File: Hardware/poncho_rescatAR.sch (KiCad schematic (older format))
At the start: 19 parts, among them P1 5V_OUT, P2 CONN_8, U1 LM317T, U2 LM7805

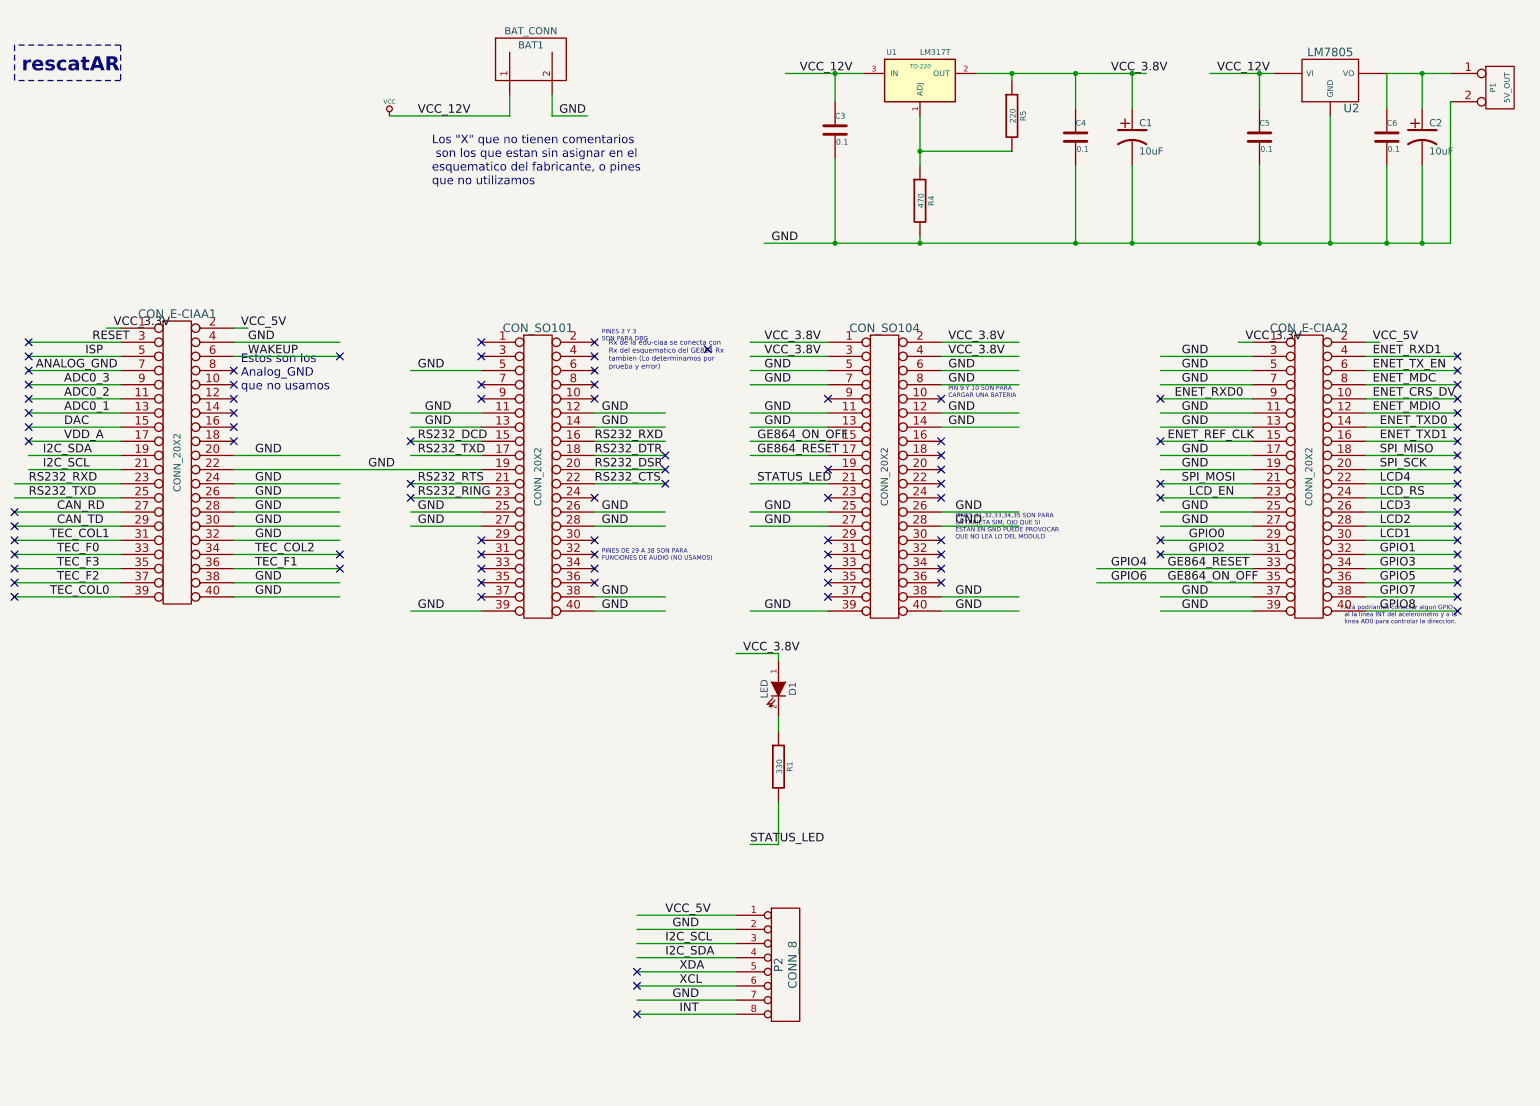
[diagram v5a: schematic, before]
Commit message: Agregado de capacitores en la alimentacion del acelerometro y pulsador de reset de la ciaa
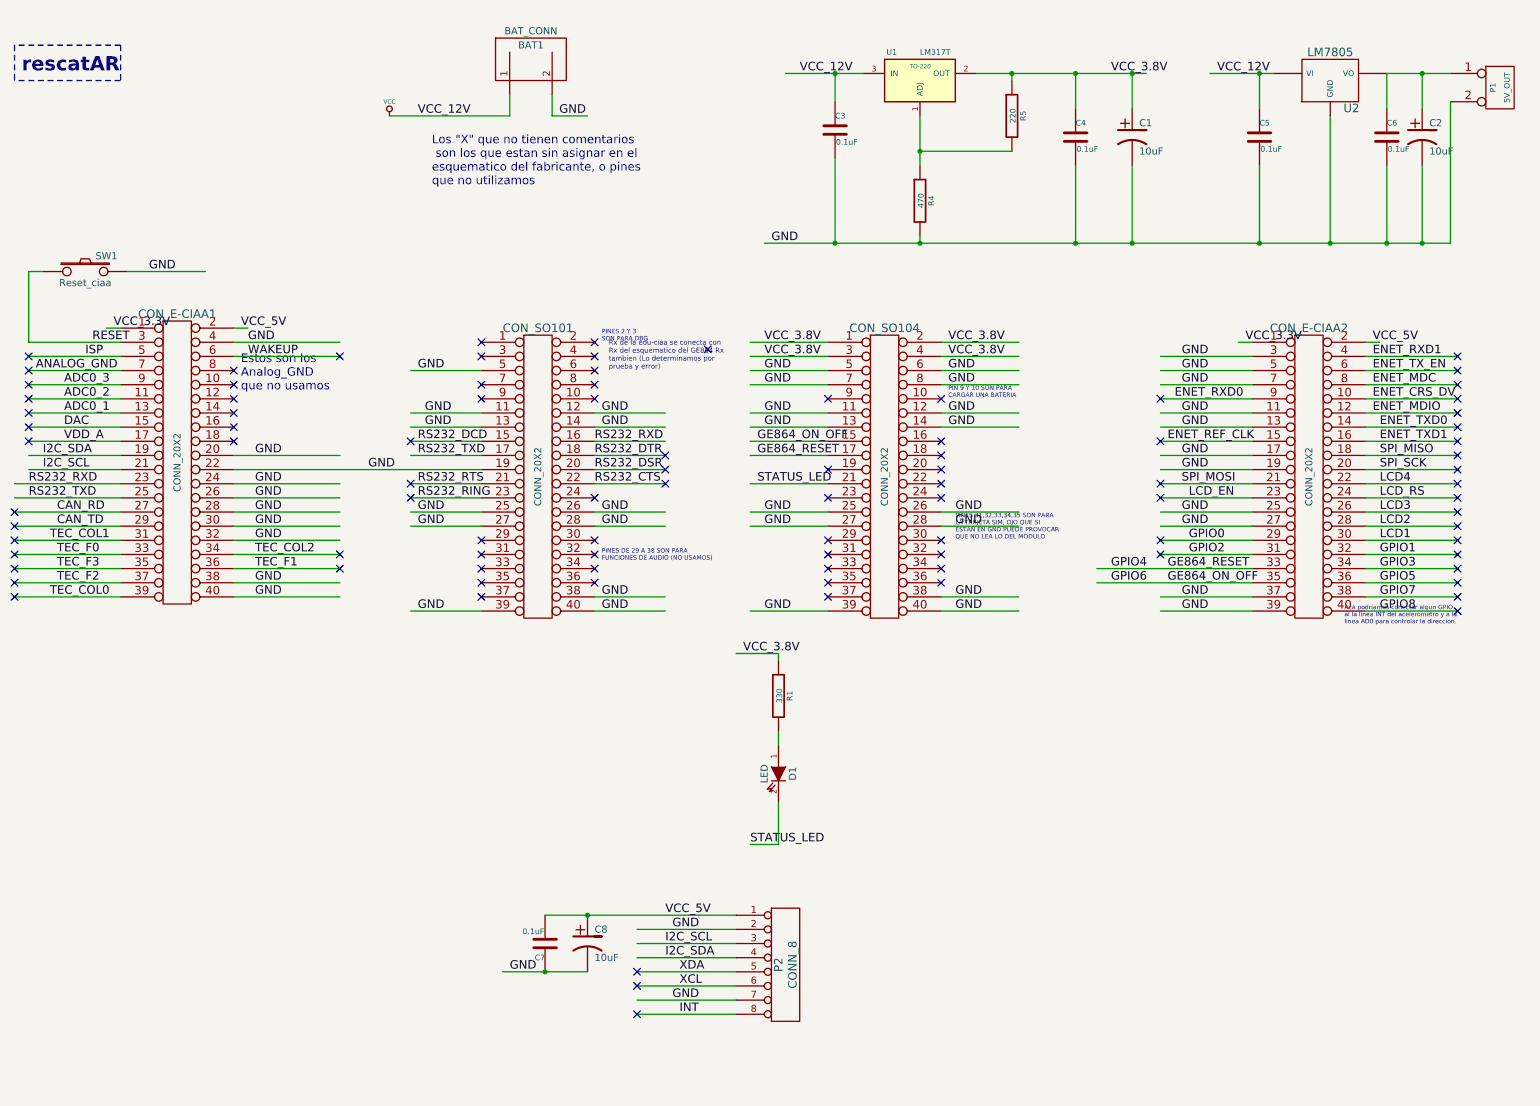
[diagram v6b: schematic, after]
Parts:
- added C7: 0.1uF, ~, symbol C
- added C8: 10uF, ~, symbol CP1
- added SW1: Reset_ciaa, ~, symbol SW_PUSH
- C3, C4, C5, C6: value 0.1 -> 0.1uF
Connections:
- wire segments 156 -> 160
- no-connect marks 96 -> 95
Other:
- moved on the sheet: D1, R1
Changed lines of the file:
@@
 LIBS:contrib
 LIBS:valves
-LIBS:w_connectors
-LIBS:bc338
 LIBS:poncho_rescatAR-cache
 EELAYER 27 0
@@
 Sheet 1 1
 Title "poncho_rescatAR"
-Date "2 dec 2015"
+Date "3 dec 2015"
 Rev "0.1"
 Comp ""
@@
 L LED D1
 U 1 1 5617B2D6
-P 6000 5150
-F 0 "D1" H 6000 5250 50  0000 C CNN
-F 1 "LED" H 6000 5050 50  0000 C CNN
-F 2 "~" H 6000 5150 60  0000 C CNN
-F 3 "~" H 6000 5150 60  0000 C CNN
-	1    6000 5150
+P 6000 5750
+F 0 "D1" H 6000 5850 50  0000 C CNN
+F 1 "LED" H 6000 5650 50  0000 C CNN
+F 2 "~" H 6000 5750 60  0000 C CNN
+F 3 "~" H 6000 5750 60  0000 C CNN
+	1    6000 5750
 	0    1    1    0
 $EndComp
 Text Label 5800 6250 0    60   ~ 0
 STATUS_LED
-NoConn ~ 700  2700
 NoConn ~ 700  2800
 NoConn ~ 700  3000
@@
 P 8100 1250
 F 0 "C4" H 8100 1350 40  0000 L CNN
-F 1 "0.1" H 8106 1165 40  0000 L CNN
+F 1 "0.1uF" H 8106 1165 40  0000 L CNN
 F 2 "~" H 8138 1100 30  0000 C CNN
 F 3 "~" H 8100 1250 60  0000 C CNN
@@
 P 6400 1200
 F 0 "C3" H 6400 1300 40  0000 L CNN
-F 1 "0.1" H 6406 1115 40  0000 L CNN
+F 1 "0.1uF" H 6406 1115 40  0000 L CNN
 F 2 "~" H 6438 1050 30  0000 C CNN
 F 3 "~" H 6400 1200 60  0000 C CNN
@@
 P 10300 1250
 F 0 "C6" H 10300 1350 40  0000 L CNN
-F 1 "0.1" H 10306 1165 40  0000 L CNN
+F 1 "0.1uF" H 10306 1165 40  0000 L CNN
 F 2 "~" H 10338 1100 30  0000 C CNN
 F 3 "~" H 10300 1250 60  0000 C CNN
@@
 P 9400 1250
 F 0 "C5" H 9400 1350 40  0000 L CNN
-F 1 "0.1" H 9406 1165 40  0000 L CNN
+F 1 "0.1uF" H 9406 1165 40  0000 L CNN
 F 2 "~" H 9438 1100 30  0000 C CNN
 F 3 "~" H 9400 1250 60  0000 C CNN
@@
 	5700 6850 5000 6850
 Wire Wire Line
-	5000 6750 5700 6750
+	4350 6750 5700 6750
 Wire Wire Line
 	1350 3600 700  3600
@@
 	7000 1100 7000 1450
 Wire Wire Line
-	7000 1950 7000 2000
+	7000 2000 7000 1950
 Wire Wire Line
 	5900 2000 10750 2000
 Wire Wire Line
-	6600 800  6050 800
+	6050 800  6600 800
 Wire Wire Line
 	7650 1350 7000 1350
@@
 Connection ~ 7000 2000
 Wire Wire Line
-	9500 800  9050 800
+	9050 800  9500 800
 Wire Wire Line
 	10550 1450 10550 2000
@@
 L R R1
 U 1 1 565EF363
-P 6000 5700
-F 0 "R1" V 6080 5700 40  0000 C CNN
-F 1 "330" V 6007 5701 40  0000 C CNN
-F 2 "~" V 5930 5700 30  0000 C CNN
-F 3 "~" H 6000 5700 30  0000 C CNN
-	1    6000 5700
-	1    0    0    -1
-$EndComp
-Wire Wire Line
-	6000 5350 6000 5450
+P 6000 5200
+F 0 "R1" V 6080 5200 40  0000 C CNN
+F 1 "330" V 6007 5201 40  0000 C CNN
+F 2 "~" V 5930 5200 30  0000 C CNN
+F 3 "~" H 6000 5200 30  0000 C CNN
+	1    6000 5200
+	1    0    0    -1
+$EndComp
 Text Label 5750 4900 0    60   ~ 0
 VCC_3.8V
@@
 	8500 1050 8500 800
 Connection ~ 8500 800
+Wire Wire Line
+	6000 5450 6000 5550
+$Comp
+L SW_PUSH SW1
+U 1 1 5660908B
+P 1100 2200
+F 0 "SW1" H 1250 2310 50  0000 C CNN
+F 1 "Reset_ciaa" H 1100 2120 50  0000 C CNN
+F 2 "~" H 1100 2200 60  0000 C CNN
+F 3 "~" H 1100 2200 60  0000 C CNN
+	1    1100 2200
+	1    0    0    -1
+$EndComp
+Wire Wire Line
+	700  2700 700  2200
+Wire Wire Line
+	700  2200 800  2200
+Wire Wire Line
+	1400 2200 1950 2200
+Text Label 1550 2200 0    60   ~ 0
+GND
+$Comp
+L C C7
+U 1 1 5660923F
+P 4350 6950
+F 0 "C7" H 4350 7050 40  0000 L CNN
+F 1 "0.1uF" H 4356 6865 40  0000 L CNN
+F 2 "~" H 4388 6800 30  0000 C CNN
+F 3 "~" H 4350 6950 60  0000 C CNN
+	1    4350 6950
+	-1   0    0    1
+$EndComp
+$Comp
+L CP1 C8
+U 1 1 5660924E
+P 4650 6950
+F 0 "C8" H 4700 7050 50  0000 L CNN
+F 1 "10uF" H 4700 6850 50  0000 L CNN
+F 2 "~" H 4650 6950 60  0000 C CNN
+F 3 "~" H 4650 6950 60  0000 C CNN
+	1    4650 6950
+	1    0    0    -1
+$EndComp
+Wire Wire Line
+	4650 7150 4050 7150
+Text Label 4100 7150 0    60   ~ 0
+GND
+Connection ~ 4650 6750
+Connection ~ 4350 7150
 $EndSCHEMATC
